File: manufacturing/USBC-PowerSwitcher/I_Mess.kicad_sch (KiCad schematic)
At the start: 5 parts, among them U3 INA180A2

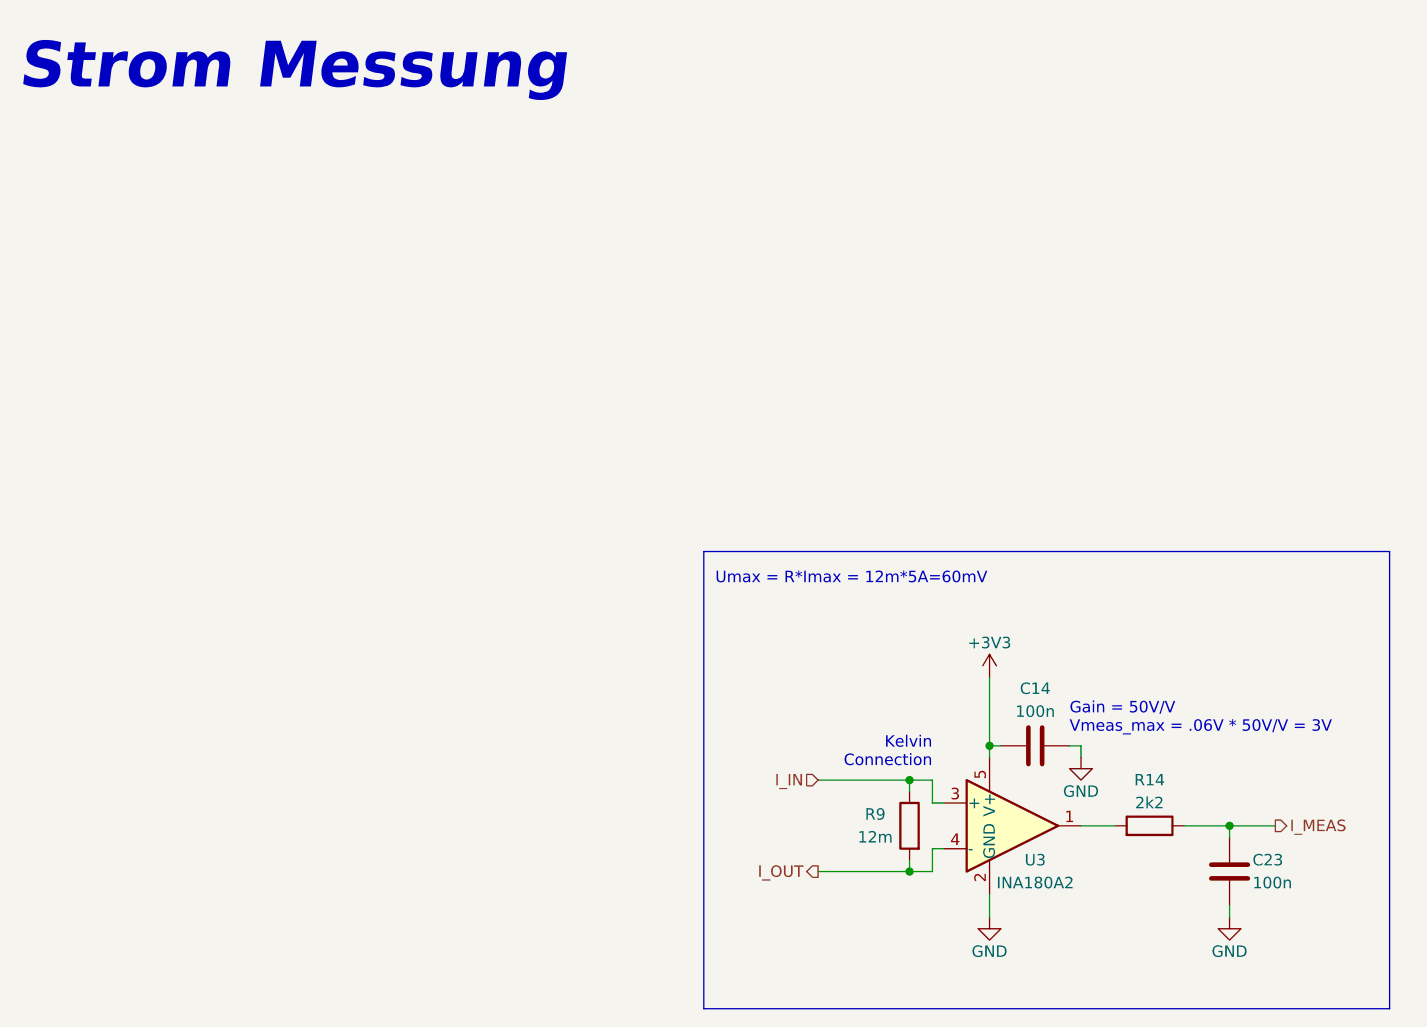
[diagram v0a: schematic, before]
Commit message: First Rough placement
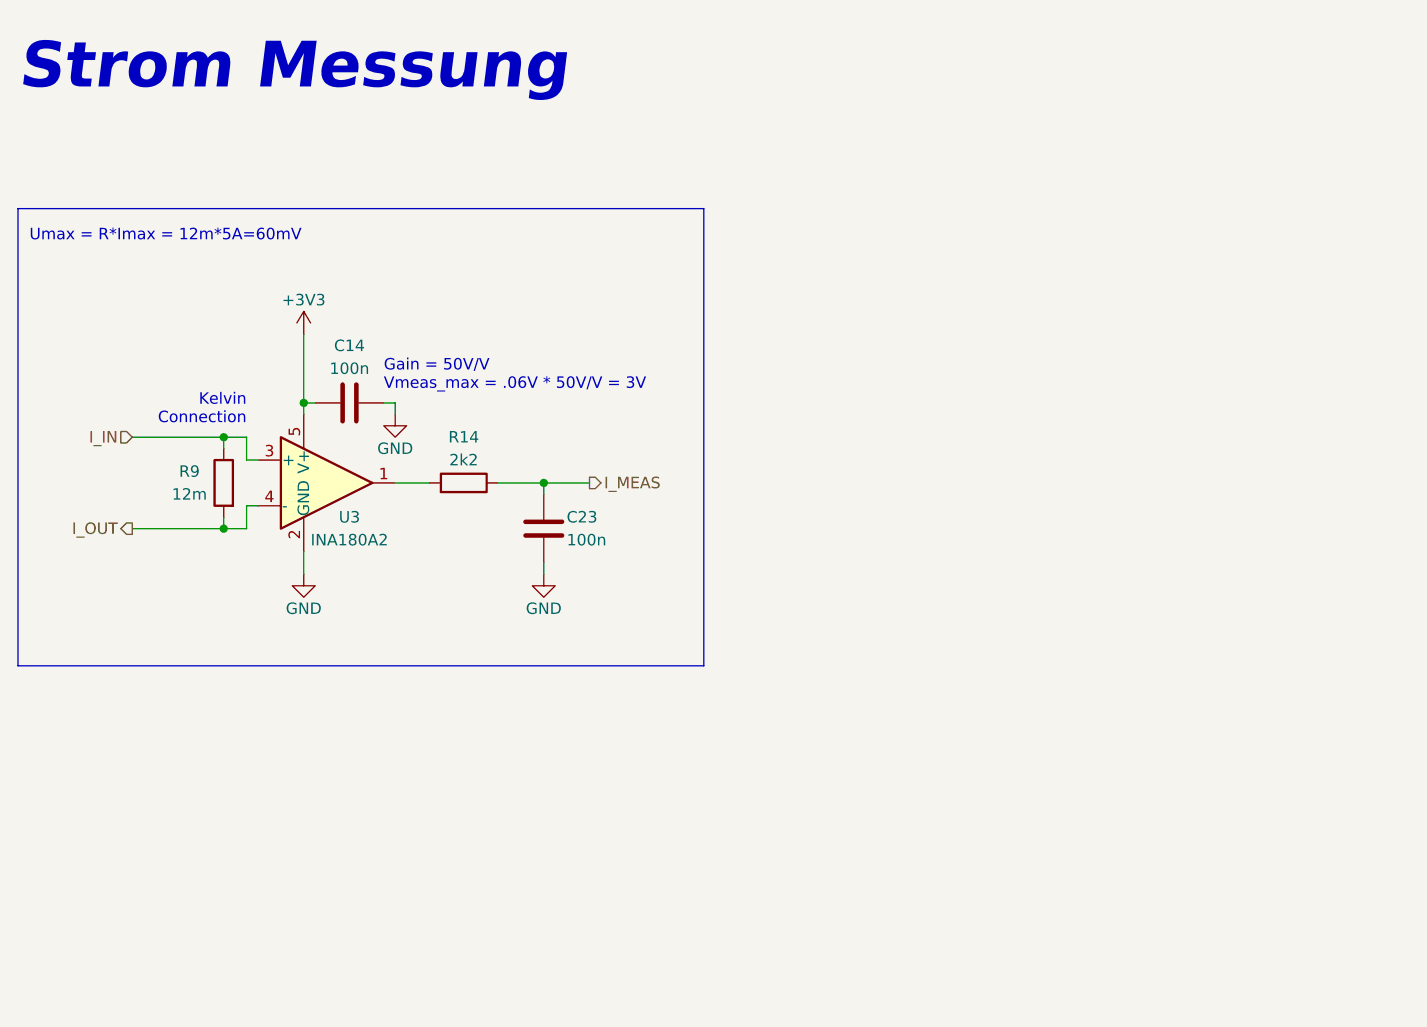
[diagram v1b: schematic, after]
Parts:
- C14, C23: footprint (none) -> Capacitor_SMD:C_0402_1005Metric; LCSC # (none) -> C307331
- R14: footprint (none) -> Resistor_SMD:R_0402_1005Metric; LCSC # (none) -> C25879
- R9: footprint (none) -> Resistor_SMD:R_2512_6332Metric; LCSC # (none) -> C5121107
- U3: LCSC # (none) -> C2059691
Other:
- moved on the sheet: C14, C23, R14, R9, U3
